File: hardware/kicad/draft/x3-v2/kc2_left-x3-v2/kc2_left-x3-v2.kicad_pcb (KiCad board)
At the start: 2 copper layers, 135.1 x 122.5 mm, 75 parts, among them SW1 KEY_01, SW10 KEY_10, SW11 KEY_11, SW12 KEY_12, SW13 KEY_13, SW14 KEY_14, SW15 KEY_15, SW16 KEY_16, SW17 KEY_17, SW18 KEY_18, SW19 KEY_19, SW2 KEY_02, SW20 KEY_20, SW21 KEY_21, SW22 KEY_22, SW23 KEY_23, SW24 KEY_24, SW25 KEY_25, SW26 KEY_26, SW27 KEY_27, SW28 KEY_28, SW29 KEY_29, SW3 KEY_03, SW30 KEY_30, SW31 KEY_31, SW4 KEY_04, SW5 KEY_05, SW6 KEY_06, SW7 KEY_07, SW8 KEY_08, SW9 KEY_09, U1 nice!nano_v2_socket_24pin

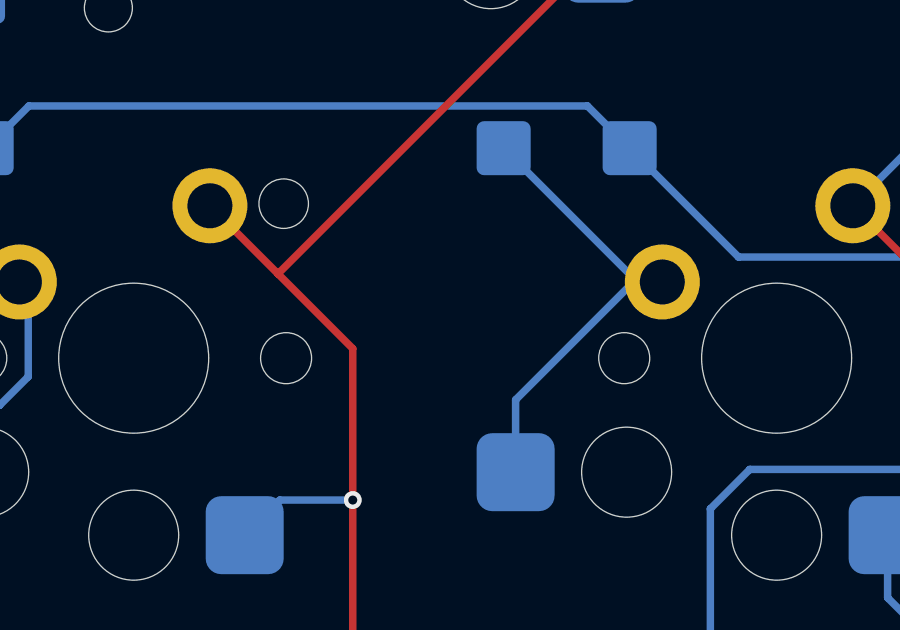
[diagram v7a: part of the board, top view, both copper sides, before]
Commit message: feat(x3-v2): reinforce mounting holes
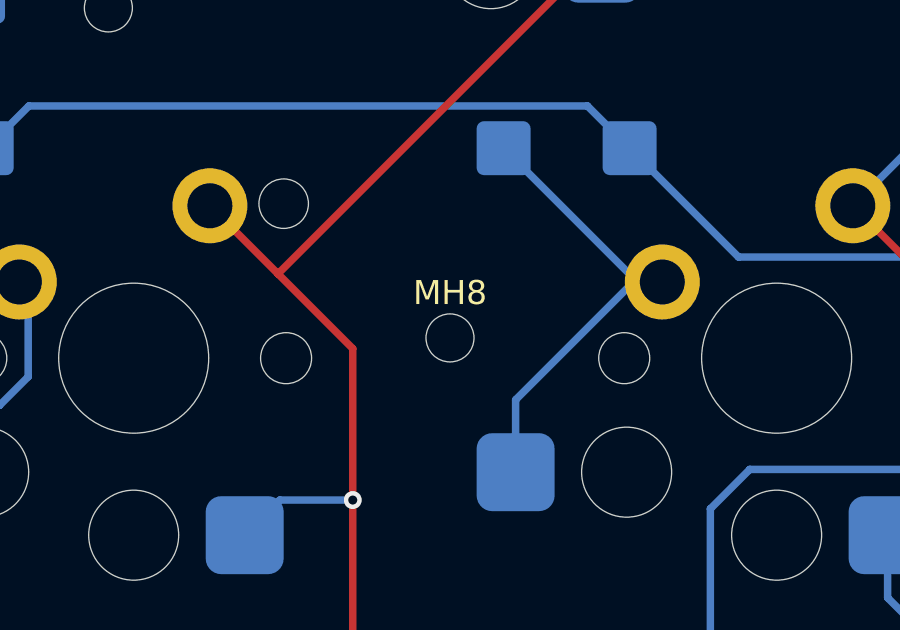
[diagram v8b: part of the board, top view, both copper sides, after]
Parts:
- added MH8: M1.4_NPTH_1.60, MH_M1.4_NPTH_1.60, F.Cu at (75.0, 134.0)
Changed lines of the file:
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@@
+		(embedded_fonts no)
+	)
+	(footprint "MH_M1.4_NPTH_1.60"
+		(layer "F.Cu")
+		(at 75 134)
+		(descr "KC2 X3 V2 M1.4 service mounting hole, 1.60 mm copper-free NPTH")
+		(tags "KC2 X3 V2 M1.4 mounting NPTH copper-free")
+		(property "Reference" "MH8"
+			(at 0 -1.5 0)
+			(layer "F.SilkS")
+			(effects
+				(font
+					(size 0.8 0.8)
+					(thickness 0.15)
+				)
+			)
+		)
+		(property "Value" "M1.4_NPTH_1.60"
+			(at 0 0 0)
+			(layer "F.Fab")
+			(hide yes)
+			(effects
+				(font
+					(size 0.8 0.8)
+					(thickness 0.1)
+				)
+			)
+		)
+		(property "Datasheet" ""
+			(at 0 0 0)
+			(layer "F.Fab")
+			(hide yes)
+			(effects
+				(font
+					(size 1.27 1.27)
+				)
+			)
+		)
+		(property "Description" ""
+			(at 0 0 0)
+			(layer "F.Fab")
+			(hide yes)
+			(effects
+				(font
+					(size 1.27 1.27)
+				)
+			)
+		)
+		(attr exclude_from_pos_files exclude_from_bom)
+		(duplicate_pad_numbers_are_jumpers no)
+		(pad "" np_thru_hole circle
+			(at 0 0)
+			(size 1.6 1.6)
+			(drill 1.6)
+			(layers "*.Mask")
+		)
 		(embedded_fonts no)
 	)
